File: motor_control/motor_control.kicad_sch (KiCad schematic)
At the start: 12 parts, among them J1 GPIO, SW1 PULLUP, SW2 PULLDOWN

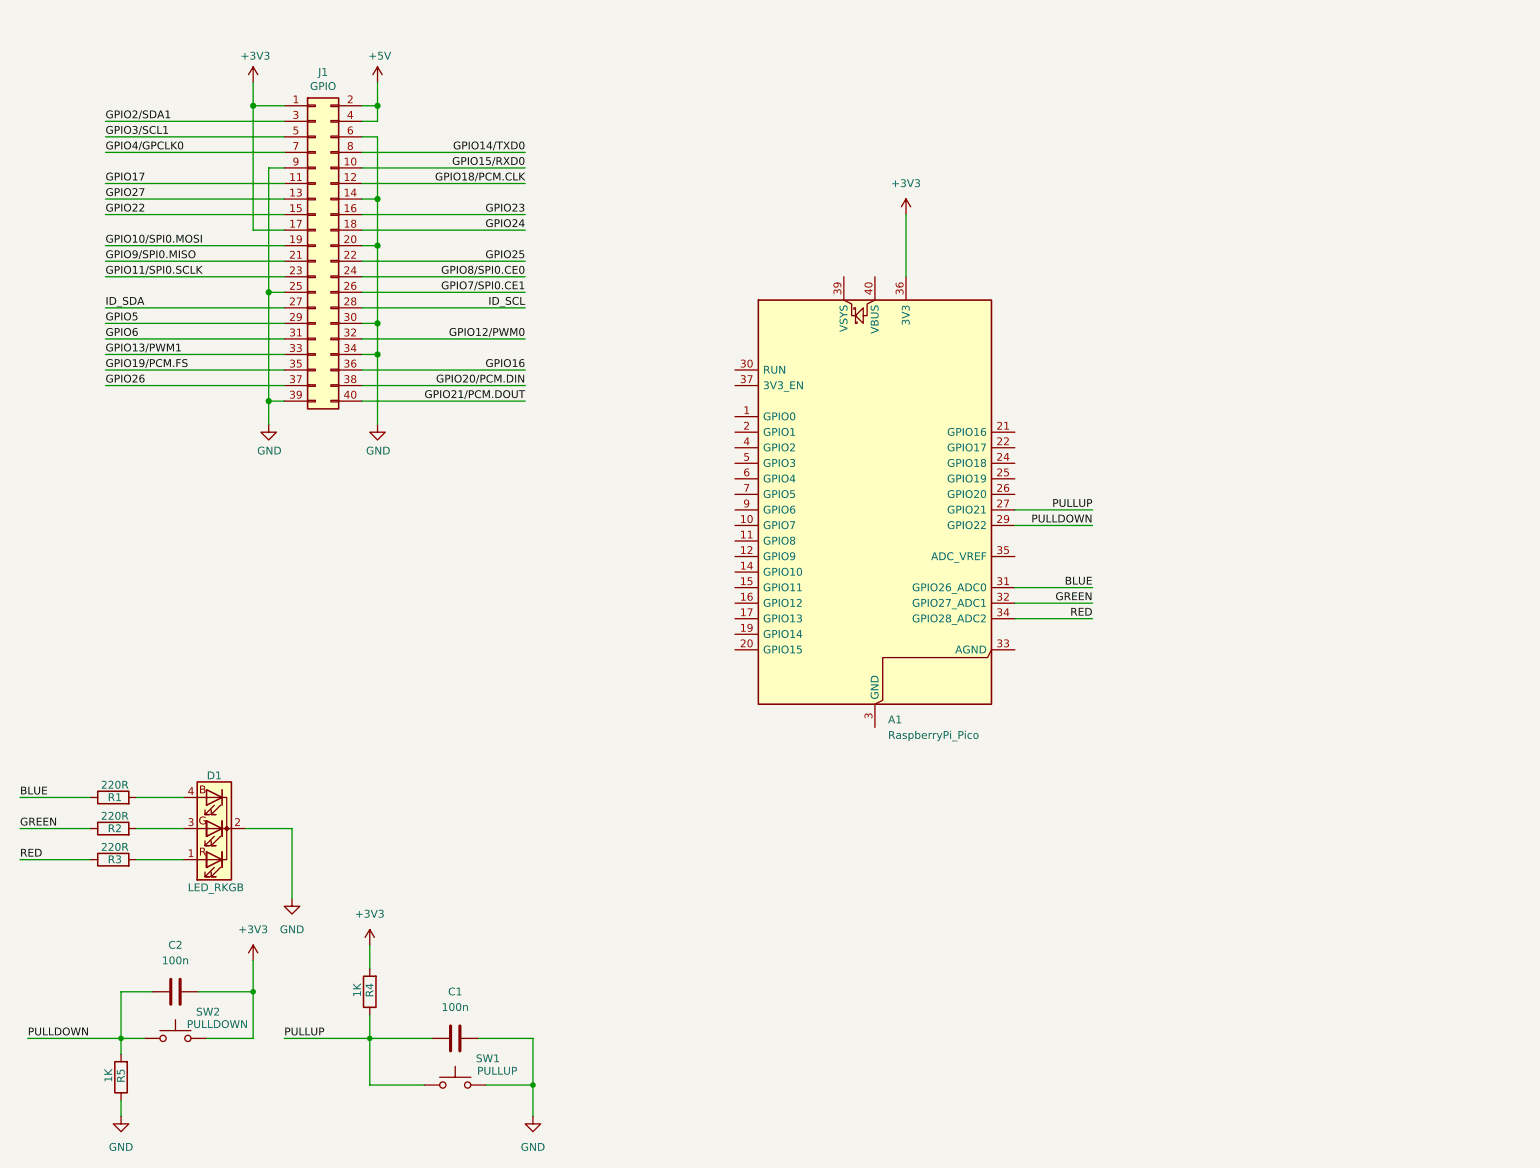
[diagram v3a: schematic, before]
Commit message: update schematic with ultrasound sensor
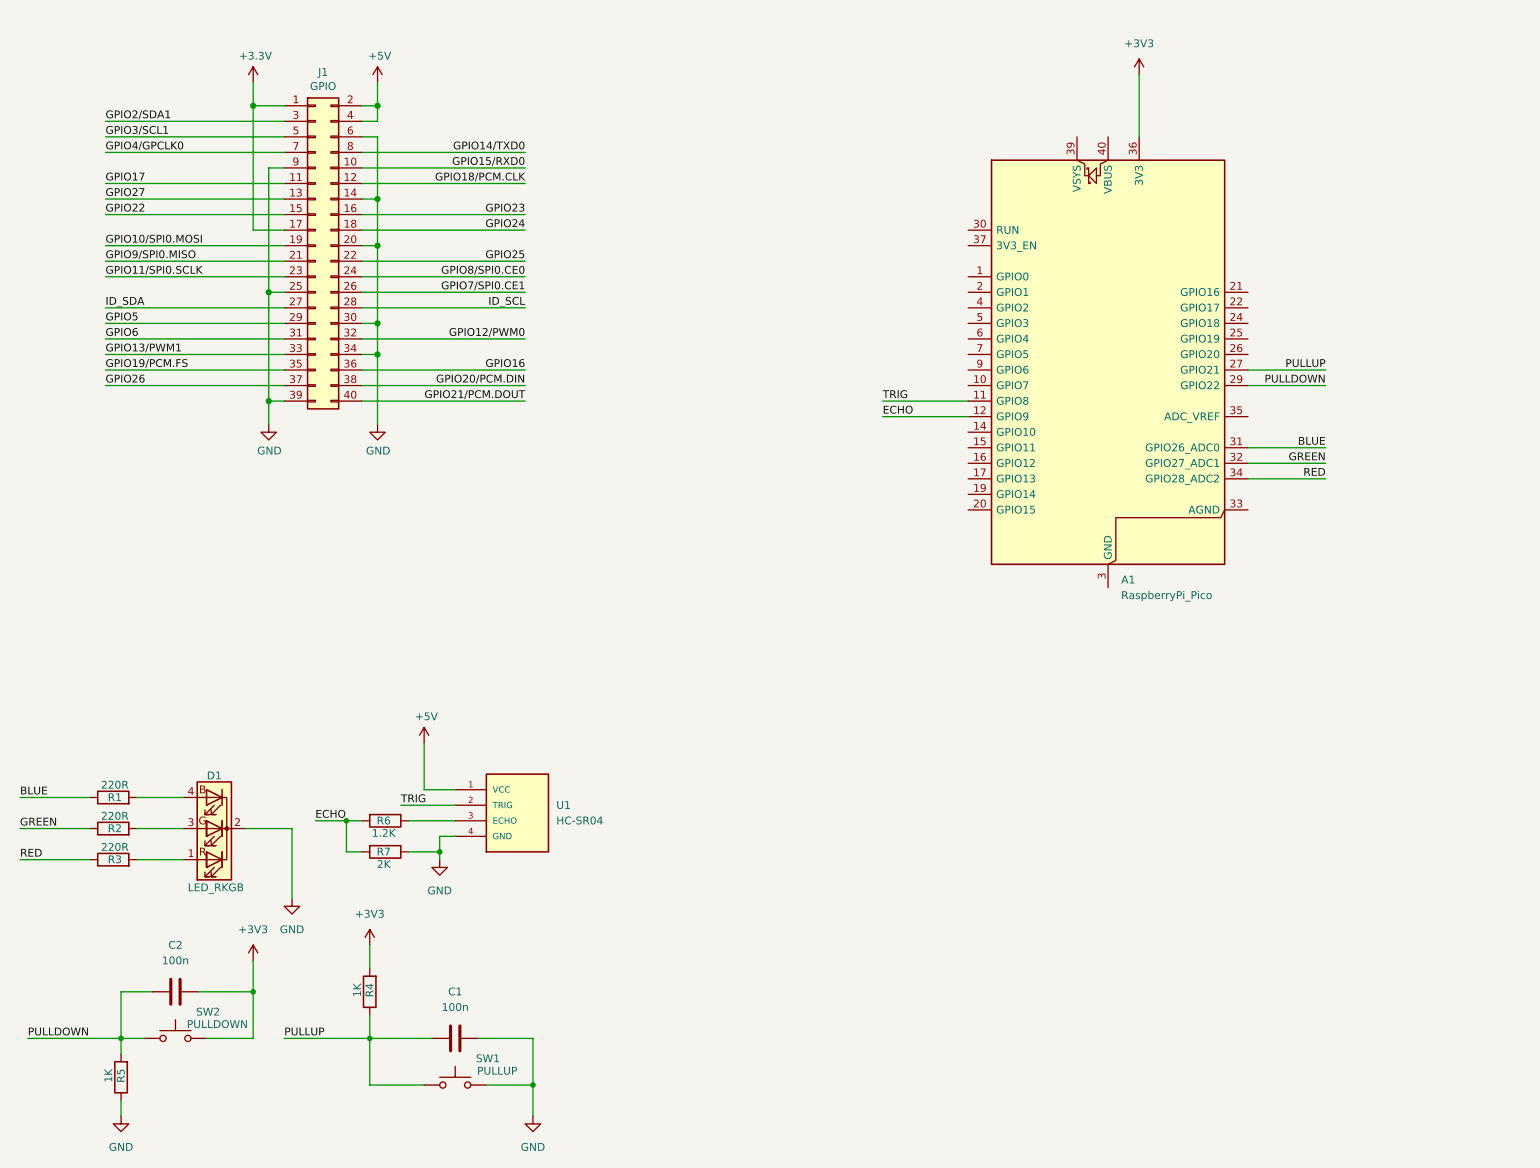
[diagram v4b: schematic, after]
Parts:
- added R6: 1.2K, symbol Device:R
- added R7: 2K, symbol Device:R
- added U1: HC-SR04, HC-SR04:XCVR_HC-SR04, symbol HC-SR04:HC-SR04
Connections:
- net +3V3: no longer J1.1 (Pin_1), J1.17 (Pin_17)
- net +5V: now also U1.1 (VCC)
- net GND: now also R7.1, U1.4 (GND)
- net TRIG: now reaches A1.11 (GPIO8)
- net TRIG: now also U1.2 (TRIG)
- net ECHO: now reaches A1.12 (GPIO9)
- net ECHO: now also R6.2, R7.2
- new net: R6.1, U1.3 (ECHO)
- new net +3.3V: J1.1 (Pin_1), J1.17 (Pin_17)
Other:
- moved on the sheet: A1

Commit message: add motor driver and connectors
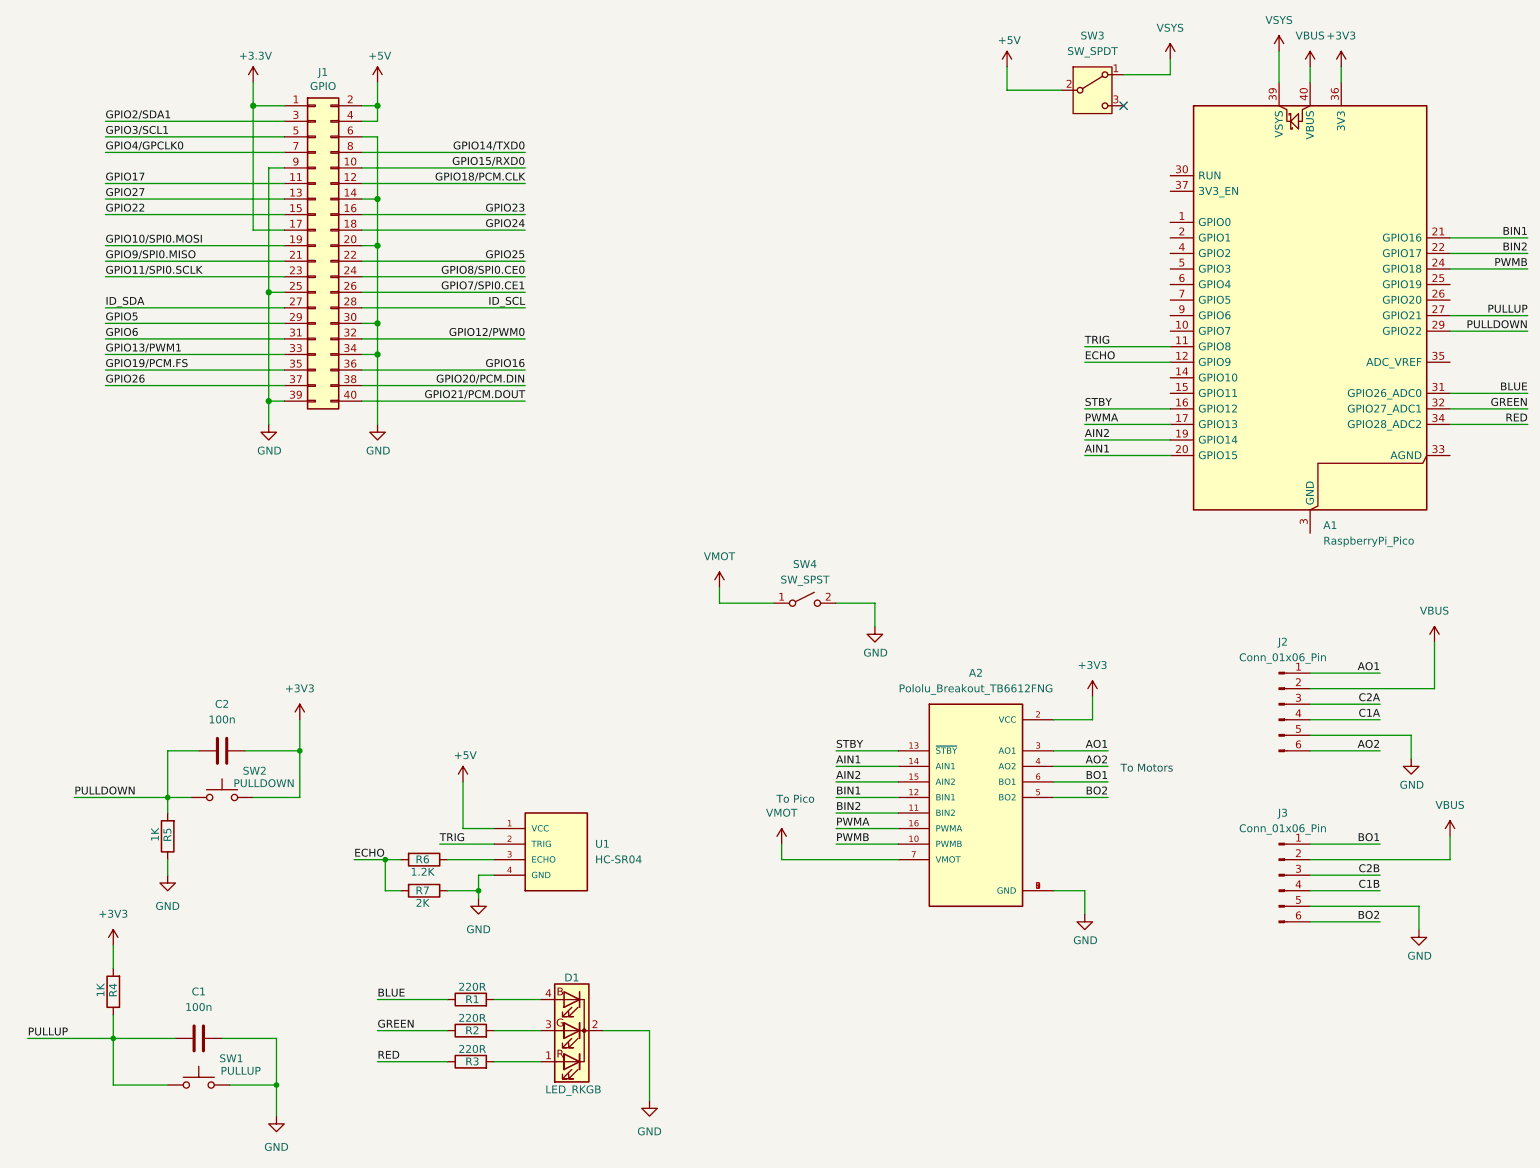
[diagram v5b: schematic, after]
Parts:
- added A2: Pololu_Breakout_TB6612FNG, POLOLU-713:SHIELD_POLOLU-713, symbol POLOLU-713:TB6612FNG_Breakout
- added J2, J3: Conn_01x06_Pin, symbol Connector:Conn_01x06_Pin
- added SW3: SW_SPDT, symbol Switch:SW_SPDT
- added SW4: SW_SPST, symbol Switch:SW_SPST
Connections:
- net +3V3: now also A2.2 (VCC)
- net +5V: now also SW3.2 (B)
- net GND: now also A2.1 (GND), A2.8 (GND), A2.9 (GND), J2.5 (Pin_5), J3.5 (Pin_5), SW4.2 (B)
- net STBY: now reaches A1.16 (GPIO12)
- net STBY: now also A2.13 (~{STBY})
- net PWMA: now reaches A1.17 (GPIO13)
- net PWMA: now also A2.16 (PWMA)
- net AIN2: now reaches A1.19 (GPIO14)
- net AIN2: now also A2.15 (AIN2)
- net AIN1: now reaches A1.20 (GPIO15)
- net AIN1: now also A2.14 (AIN1)
- net BIN1: now reaches A1.21 (GPIO16)
- net BIN1: now also A2.12 (BIN1)
- net BIN2: now reaches A1.22 (GPIO17)
- net BIN2: now also A2.11 (BIN2)
- net PWMB: now reaches A1.24 (GPIO18)
- net PWMB: now also A2.10 (PWMB)
- net VSYS: now reaches A1.39 (VSYS)
- net VSYS: now also SW3.1 (A)
- net VBUS: now reaches A1.40 (VBUS)
- net VBUS: now also J2.2 (Pin_2), J3.2 (Pin_2)
- new net AO1: A2.3 (AO1), J2.1 (Pin_1)
- new net AO2: A2.4 (AO2), J2.6 (Pin_6)
- new net BO1: A2.6 (BO1), J3.1 (Pin_1)
- new net BO2: A2.5 (BO2), J3.6 (Pin_6)
- new net C1A: J2.4 (Pin_4)
- new net C1B: J3.4 (Pin_4)
- new net C2A: J2.3 (Pin_3)
- new net C2B: J3.3 (Pin_3)
- new net VMOT: A2.7 (VMOT), SW4.1 (A)
- no-connect marks 0 -> 1
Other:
- note added: "To Motors"
- note added: "To Pico"
- moved on the sheet: A1, C1, C2, D1, R1, R2, R3, R4, R5, R6, R7, SW1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

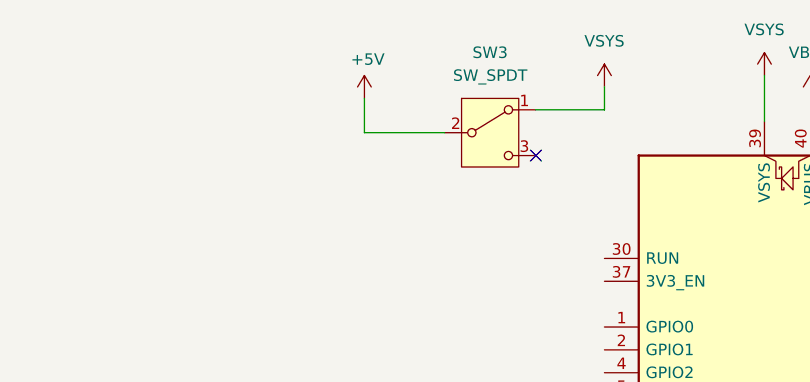
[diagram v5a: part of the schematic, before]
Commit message: replace switch with a jumper
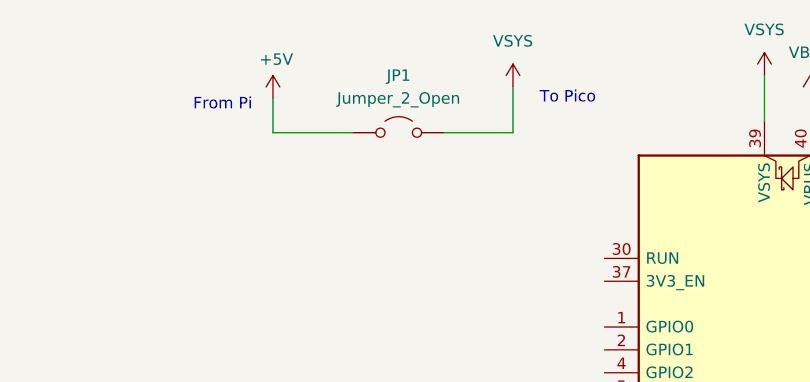
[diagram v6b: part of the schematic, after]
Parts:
- removed SW3: SW_SPDT, symbol Switch:SW_SPDT
- added JP1: Jumper_2_Open, symbol Jumper:Jumper_2_Open
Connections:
- net +5V: now also JP1.1 (A)
- net VSYS: now also JP1.2 (B)
- no-connect marks 1 -> 0
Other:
- note added: "From Pi"
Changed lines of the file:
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@@
 		(company "UCA")
 	)
+	(text "From Pi"
+		(exclude_from_sim no)
+		(at 163.322 22.352 0)
+		(effects
+			(font
+				(size 1.27 1.27)
+			)
+		)
+	)
 	(text "To Motors"
 		(exclude_from_sim no)
@@
 		)
 	)
+	(text "To Pico"
+		(exclude_from_sim no)
+		(at 201.676 21.59 0)
+		(effects
+			(font
+				(size 1.27 1.27)
+			)
+		)
+	)
 	(junction
 		(at 59.69 187.96)
@@
 		(color 0 0 0 0)
 	)
-	(no_connect
-		(at 198.12 27.94)
-	)
 	(wire
 		(pts
@@
 	(wire
 		(pts
+			(xy 195.58 25.4) (xy 195.58 20.32)
+		)
+		(stroke
+			(width 0)
+			(type default)
+		)
+	)
+	(wire
+		(pts
 			(xy 186.69 128.27) (xy 193.04 128.27)
 		)
@@
 	(wire
 		(pts
-			(xy 179.07 25.4) (xy 187.96 25.4)
-		)
-		(stroke
-			(width 0)
-			(type default)
-		)
-	)
-	(wire
-		(pts
 			(xy 132.08 109.22) (xy 140.97 109.22)
 		)
@@
 	(wire
 		(pts
-			(xy 205.74 22.86) (xy 205.74 20.32)
-		)
-		(stroke
-			(width 0)
-			(type default)
-		)
-	)
-	(wire
-		(pts
 			(xy 90.17 146.05) (xy 95.25 146.05)
 		)
@@
 	(wire
 		(pts
-			(xy 179.07 21.59) (xy 179.07 25.4)
-		)
-		(stroke
-			(width 0)
-			(type default)
-		)
-	)
-	(wire
-		(pts
 			(xy 73.66 73.66) (xy 100.33 73.66)
 		)
@@
 	(wire
 		(pts
-			(xy 198.12 22.86) (xy 205.74 22.86)
-		)
-		(stroke
-			(width 0)
-			(type default)
-		)
-	)
-	(wire
-		(pts
 			(xy 31.75 73.66) (xy 60.96 73.66)
 		)
@@
 	(wire
 		(pts
+			(xy 168.91 21.59) (xy 168.91 25.4)
+		)
+		(stroke
+			(width 0)
+			(type default)
+		)
+	)
+	(wire
+		(pts
 			(xy 228.6 153.67) (xy 240.03 153.67)
 		)
@@
 	(wire
 		(pts
+			(xy 187.96 25.4) (xy 195.58 25.4)
+		)
+		(stroke
+			(width 0)
+			(type default)
+		)
+	)
+	(wire
+		(pts
 			(xy 76.2 68.58) (xy 76.2 80.01)
 		)
@@
 	(wire
 		(pts
+			(xy 168.91 25.4) (xy 177.8 25.4)
+		)
+		(stroke
+			(width 0)
+			(type default)
+		)
+	)
+	(wire
+		(pts
 			(xy 248.92 123.19) (xy 228.6 123.19)
 		)
@@
 	)
 	(symbol
-		(lib_id "Switch:SW_SPDT")
-		(at 193.04 25.4 0)
-		(unit 1)
-		(exclude_from_sim no)
-		(in_bom yes)
-		(on_board yes)
-		(dnp no)
-		(fields_autoplaced yes)
-		(property "Reference" "SW3"
-			(at 193.04 16.51 0)
-			(effects
-				(font
-					(size 1.27 1.27)
-				)
-			)
-		)
-		(property "Value" "SW_SPDT"
-			(at 193.04 19.05 0)
-			(effects
-				(font
-					(size 1.27 1.27)
-				)
-			)
-		)
-		(property "Footprint" ""
-			(at 193.04 25.4 0)
-			(effects
-				(font
-					(size 1.27 1.27)
-				)
-				(hide yes)
-			)
-		)
-		(property "Datasheet" "~"
-			(at 193.04 33.02 0)
-			(effects
-				(font
-					(size 1.27 1.27)
-				)
-				(hide yes)
-			)
-		)
-		(property "Description" "Switch, single pole double throw"
-			(at 193.04 25.4 0)
-			(effects
-				(font
-					(size 1.27 1.27)
-				)
-				(hide yes)
-			)
-		)
-		(pin "2"
-		)
-		(pin "1"
-		)
-		(pin "3"
-		)
-		(instances
-			(project ""
-				(path "/e63e39d7-6ac0-4ffd-8aa3-1841a4541b55"
-					(reference "SW3")
-					(unit 1)
-				)
-			)
-		)
-	)
-	(symbol
 		(lib_id "Device:LED_RKGB")
 		(at 107.95 179.07 180)
@@
 	(symbol
 		(lib_id "power:+5V")
-		(at 179.07 21.59 0)
+		(at 168.91 21.59 0)
 		(unit 1)
 		(exclude_from_sim no)
@@
 		(dnp no)
 		(property "Reference" "#PWR013"
-			(at 179.07 25.4 0)
+			(at 168.91 25.4 0)
 			(effects
 				(font
@@
 		)
 		(property "Value" "+5V"
-			(at 179.4383 17.2656 0)
+			(at 169.2783 17.2656 0)
 			(effects
 				(font
@@
 		)
 		(property "Footprint" ""
-			(at 179.07 21.59 0)
+			(at 168.91 21.59 0)
 			(effects
 				(font
@@
 		)
 		(property "Datasheet" ""
-			(at 179.07 21.59 0)
+			(at 168.91 21.59 0)
 			(effects
 				(font
@@
 		)
 		(property "Description" "Power symbol creates a global label with name \"+5V\""
-			(at 179.07 21.59 0)
+			(at 168.91 21.59 0)
 			(effects
 				(font
@@
 	)
 	(symbol
+		(lib_id "Jumper:Jumper_2_Open")
+		(at 182.88 25.4 0)
+		(unit 1)
+		(exclude_from_sim no)
+		(in_bom yes)
+		(on_board yes)
+		(dnp no)
+		(fields_autoplaced yes)
+		(property "Reference" "JP1"
+			(at 182.88 19.05 0)
+			(effects
+				(font
+					(size 1.27 1.27)
+				)
+			)
+		)
+		(property "Value" "Jumper_2_Open"
+			(at 182.88 21.59 0)
+			(effects
+				(font
+					(size 1.27 1.27)
+				)
+			)
+		)
+		(property "Footprint" ""
+			(at 182.88 25.4 0)
+			(effects
+				(font
+					(size 1.27 1.27)
+				)
+				(hide yes)
+			)
+		)
+		(property "Datasheet" "~"
+			(at 182.88 25.4 0)
+			(effects
+				(font
+					(size 1.27 1.27)
+				)
+				(hide yes)
+			)
+		)
+		(property "Description" "Jumper, 2-pole, open"
+			(at 182.88 25.4 0)
+			(effects
+				(font
+					(size 1.27 1.27)
+				)
+				(hide yes)
+			)
+		)
+		(pin "2"
+		)
+		(pin "1"
+		)
+		(instances
+			(project ""
+				(path "/e63e39d7-6ac0-4ffd-8aa3-1841a4541b55"
+					(reference "JP1")
+					(unit 1)
+				)
+			)
+		)
+	)
+	(symbol
 		(lib_id "power:GND")
 		(at 245.11 134.62 0)
@@
 	(symbol
 		(lib_id "power:+3V3")
-		(at 205.74 20.32 0)
+		(at 195.58 20.32 0)
 		(unit 1)
 		(exclude_from_sim no)
@@
 		(fields_autoplaced yes)
 		(property "Reference" "#PWR016"
-			(at 205.74 24.13 0)
+			(at 195.58 24.13 0)
 			(effects
 				(font
@@
 		)
 		(property "Value" "VSYS"
-			(at 205.74 15.24 0)
+			(at 195.58 15.24 0)
 			(effects
 				(font
@@
 		)
 		(property "Footprint" ""
-			(at 205.74 20.32 0)
+			(at 195.58 20.32 0)
 			(effects
 				(font
@@
 		)
 		(property "Datasheet" ""
-			(at 205.74 20.32 0)
+			(at 195.58 20.32 0)
 			(effects
 				(font
@@
 		)
 		(property "Description" "Power symbol creates a global label with name \"+3V3\""
-			(at 205.74 20.32 0)
+			(at 195.58 20.32 0)
 			(effects
 				(font
